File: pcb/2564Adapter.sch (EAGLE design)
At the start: 6 parts, among them IC1 TMS2564, IC2 EPROM

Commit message: !PGM/PD is a possible select pin, so add in required logic to handle correctly for all cases.
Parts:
- added IC4: 74LS00N, 74xx-us-jlb:74LS00N
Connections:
- removed net N$3: IC1A.!CS1, IC2G$1.!OE
- new net !CE: IC2G$1.!CE, IC4B.O
- new net !CS1: IC1A.!CS1, IC4A.I0, IC4A.I1
- new net !CS2: IC1A.!CS2, IC4D.I0, IC4D.I1
- new net GND: IC4C.I0, IC4C.I1
- new net N$2: IC4B.I1, IC4D.O
- new net PD: IC1A.PD/!PGM, IC2G$1.!OE
- net N$1: now also IC4A.O, IC4B.I0; no longer IC1A.!CS2, IC2G$1.!CE
- net VCC: no longer IC1A.!PGM
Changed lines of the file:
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@@
 <layer number="97" name="Info" color="7" fill="1" visible="yes" active="yes"/>
 <layer number="98" name="Guide" color="6" fill="1" visible="yes" active="yes"/>
+<layer number="99" name="SpiceOrder" color="5" fill="1" visible="yes" active="yes"/>
 <layer number="100" name="Muster" color="7" fill="1" visible="no" active="no"/>
 <layer number="101" name="Patch_Top" color="12" fill="4" visible="yes" active="yes"/>
@@
 <layer number="106" name="bPlate" color="7" fill="1" visible="yes" active="yes"/>
 <layer number="107" name="Crop" color="7" fill="1" visible="yes" active="yes"/>
+<layer number="110" name="OldCocoCase" color="7" fill="1" visible="yes" active="yes"/>
+<layer number="111" name="NewCocoCase" color="7" fill="1" visible="yes" active="yes"/>
+<layer number="112" name="C64Case" color="7" fill="1" visible="yes" active="yes"/>
 <layer number="116" name="Patch_BOT" color="9" fill="4" visible="yes" active="yes"/>
 <layer number="121" name="_tsilk" color="7" fill="1" visible="yes" active="yes"/>
@@
 <part name="IC2" library="0RB_Memory" deviceset="27512" device="'RD'" value="EPROM"/>
 <part name="IC1" library="memory-ti" deviceset="TMS2564" device="-RP" value="TMS2564"/>
-<part name="SUPPLY1" library="supply2" deviceset="VCC" device=""/>
 <part name="GOLD_ORB_SM1" library="oshw" deviceset="OSHWLOGO" device="LOGO5MM" value="Open Source Hardware"/>
+<part name="IC4" library="74xx-us-jlb" deviceset="74*00" device="N" technology="LS"/>
+<part name="SUPPLY1" library="supply2" deviceset="GND" device=""/>
 </parts>
 <sheets>
@@
 <instance part="IC2" gate="G$1" x="68.58" y="83.82"/>
 <instance part="IC1" gate="A" x="68.58" y="137.16"/>
-<instance part="SUPPLY1" gate="G$1" x="53.34" y="167.64"/>
 <instance part="GOLD_ORB_SM1" gate="G$1" x="134.62" y="15.24"/>
+<instance part="IC4" gate="A" x="134.62" y="114.3"/>
+<instance part="IC4" gate="B" x="165.1" y="104.14"/>
+<instance part="IC4" gate="C" x="134.62" y="68.58"/>
+<instance part="IC4" gate="D" x="134.62" y="93.98"/>
+<instance part="SUPPLY1" gate="GND" x="119.38" y="60.96"/>
 </instances>
 <busses>
@@
 <pinref part="SUPPLY2" gate="G$1" pin="VCC"/>
 </segment>
-<segment>
-<pinref part="SUPPLY1" gate="G$1" pin="VCC"/>
-<wire x1="53.34" y1="165.1" x2="53.34" y2="116.84" width="0.1524" layer="91"/>
-<pinref part="IC1" gate="A" pin="!PGM"/>
-<wire x1="55.88" y1="116.84" x2="53.34" y2="116.84" width="0.1524" layer="91"/>
-</segment>
 </net>
 <net name="A15" class="0">
@@
 </segment>
 </net>
-<net name="N$3" class="0">
-<segment>
-<wire x1="48.26" y1="121.92" x2="55.88" y2="121.92" width="0.1524" layer="91"/>
-<wire x1="48.26" y1="58.42" x2="55.88" y2="58.42" width="0.1524" layer="91"/>
-<wire x1="48.26" y1="121.92" x2="48.26" y2="58.42" width="0.1524" layer="91"/>
+<net name="!CS1" class="0">
+<segment>
+<pinref part="IC1" gate="A" pin="!CS1"/>
+<wire x1="55.88" y1="121.92" x2="38.1" y2="121.92" width="0.1524" layer="91"/>
+<label x="38.1" y="121.92" size="1.27" layer="95" ratio="10" rot="R180" xref="yes"/>
+</segment>
+<segment>
+<pinref part="IC4" gate="A" pin="I0"/>
+<wire x1="121.92" y1="116.84" x2="119.38" y2="116.84" width="0.1524" layer="91"/>
+<wire x1="119.38" y1="116.84" x2="119.38" y2="114.3" width="0.1524" layer="91"/>
+<pinref part="IC4" gate="A" pin="I1"/>
+<wire x1="119.38" y1="114.3" x2="119.38" y2="111.76" width="0.1524" layer="91"/>
+<wire x1="119.38" y1="111.76" x2="121.92" y2="111.76" width="0.1524" layer="91"/>
+<wire x1="119.38" y1="114.3" x2="116.84" y2="114.3" width="0.1524" layer="91"/>
+<junction x="119.38" y="114.3"/>
+<label x="116.84" y="114.3" size="1.27" layer="95" ratio="10" rot="R180" xref="yes"/>
+</segment>
+</net>
+<net name="!CS2" class="0">
+<segment>
+<pinref part="IC1" gate="A" pin="!CS2"/>
+<wire x1="55.88" y1="119.38" x2="38.1" y2="119.38" width="0.1524" layer="91"/>
+<label x="38.1" y="119.38" size="1.27" layer="95" ratio="10" rot="R180" xref="yes"/>
+</segment>
+<segment>
+<pinref part="IC4" gate="D" pin="I0"/>
+<wire x1="121.92" y1="96.52" x2="119.38" y2="96.52" width="0.1524" layer="91"/>
+<wire x1="119.38" y1="96.52" x2="119.38" y2="93.98" width="0.1524" layer="91"/>
+<pinref part="IC4" gate="D" pin="I1"/>
+<wire x1="119.38" y1="93.98" x2="119.38" y2="91.44" width="0.1524" layer="91"/>
+<wire x1="119.38" y1="91.44" x2="121.92" y2="91.44" width="0.1524" layer="91"/>
+<wire x1="119.38" y1="93.98" x2="116.84" y2="93.98" width="0.1524" layer="91"/>
+<junction x="119.38" y="93.98"/>
+<label x="116.84" y="93.98" size="1.27" layer="95" ratio="10" rot="R180" xref="yes"/>
+</segment>
+</net>
+<net name="PD" class="0">
+<segment>
+<pinref part="IC1" gate="A" pin="PD/!PGM"/>
+<wire x1="55.88" y1="116.84" x2="38.1" y2="116.84" width="0.1524" layer="91"/>
+<label x="38.1" y="116.84" size="1.27" layer="95" ratio="10" rot="R180" xref="yes"/>
+</segment>
+<segment>
 <pinref part="IC2" gate="G$1" pin="!OE"/>
-<pinref part="IC1" gate="A" pin="!CS1"/>
+<wire x1="38.1" y1="58.42" x2="55.88" y2="58.42" width="0.1524" layer="91"/>
+<label x="38.1" y="58.42" size="1.27" layer="95" ratio="10" rot="R180" xref="yes"/>
+</segment>
+</net>
+<net name="!CE" class="0">
+<segment>
+<pinref part="IC2" gate="G$1" pin="!CE"/>
+<wire x1="55.88" y1="60.96" x2="38.1" y2="60.96" width="0.1524" layer="91"/>
+<label x="38.1" y="60.96" size="1.27" layer="95" ratio="10" rot="R180" xref="yes"/>
+</segment>
+<segment>
+<pinref part="IC4" gate="B" pin="O"/>
+<wire x1="177.8" y1="104.14" x2="180.34" y2="104.14" width="0.1524" layer="91"/>
+<label x="180.34" y="104.14" size="1.27" layer="95" ratio="10" xref="yes"/>
 </segment>
 </net>
 <net name="N$1" class="0">
 <segment>
-<pinref part="IC2" gate="G$1" pin="!CE"/>
-<pinref part="IC1" gate="A" pin="!CS2"/>
-<wire x1="55.88" y1="119.38" x2="50.8" y2="119.38" width="0.1524" layer="91"/>
-<wire x1="50.8" y1="119.38" x2="50.8" y2="60.96" width="0.1524" layer="91"/>
-<wire x1="50.8" y1="60.96" x2="55.88" y2="60.96" width="0.1524" layer="91"/>
-</segment>
-</net>
+<pinref part="IC4" gate="A" pin="O"/>
+<wire x1="147.32" y1="114.3" x2="149.86" y2="114.3" width="0.1524" layer="91"/>
+<wire x1="149.86" y1="114.3" x2="149.86" y2="106.68" width="0.1524" layer="91"/>
+<pinref part="IC4" gate="B" pin="I0"/>
+<wire x1="149.86" y1="106.68" x2="152.4" y2="106.68" width="0.1524" layer="91"/>
+</segment>
+</net>
+<net name="N$2" class="0">
+<segment>
+<pinref part="IC4" gate="B" pin="I1"/>
+<wire x1="152.4" y1="101.6" x2="149.86" y2="101.6" width="0.1524" layer="91"/>
+<wire x1="149.86" y1="101.6" x2="149.86" y2="93.98" width="0.1524" layer="91"/>
+<pinref part="IC4" gate="D" pin="O"/>
+<wire x1="149.86" y1="93.98" x2="147.32" y2="93.98" width="0.1524" layer="91"/>
+</segment>
+</net>
+<net name="GND" class="0">
+<segment>
+<pinref part="IC4" gate="C" pin="I0"/>
+<wire x1="121.92" y1="71.12" x2="119.38" y2="71.12" width="0.1524" layer="91"/>
+<wire x1="119.38" y1="71.12" x2="119.38" y2="66.04" width="0.1524" layer="91"/>
+<pinref part="SUPPLY1" gate="GND" pin="GND"/>
+<pinref part="IC4" gate="C" pin="I1"/>
+<wire x1="119.38" y1="66.04" x2="119.38" y2="63.5" width="0.1524" layer="91"/>
+<wire x1="121.92" y1="66.04" x2="119.38" y2="66.04" width="0.1524" layer="91"/>
+<junction x="119.38" y="66.04"/>
+</segment>
+</net>

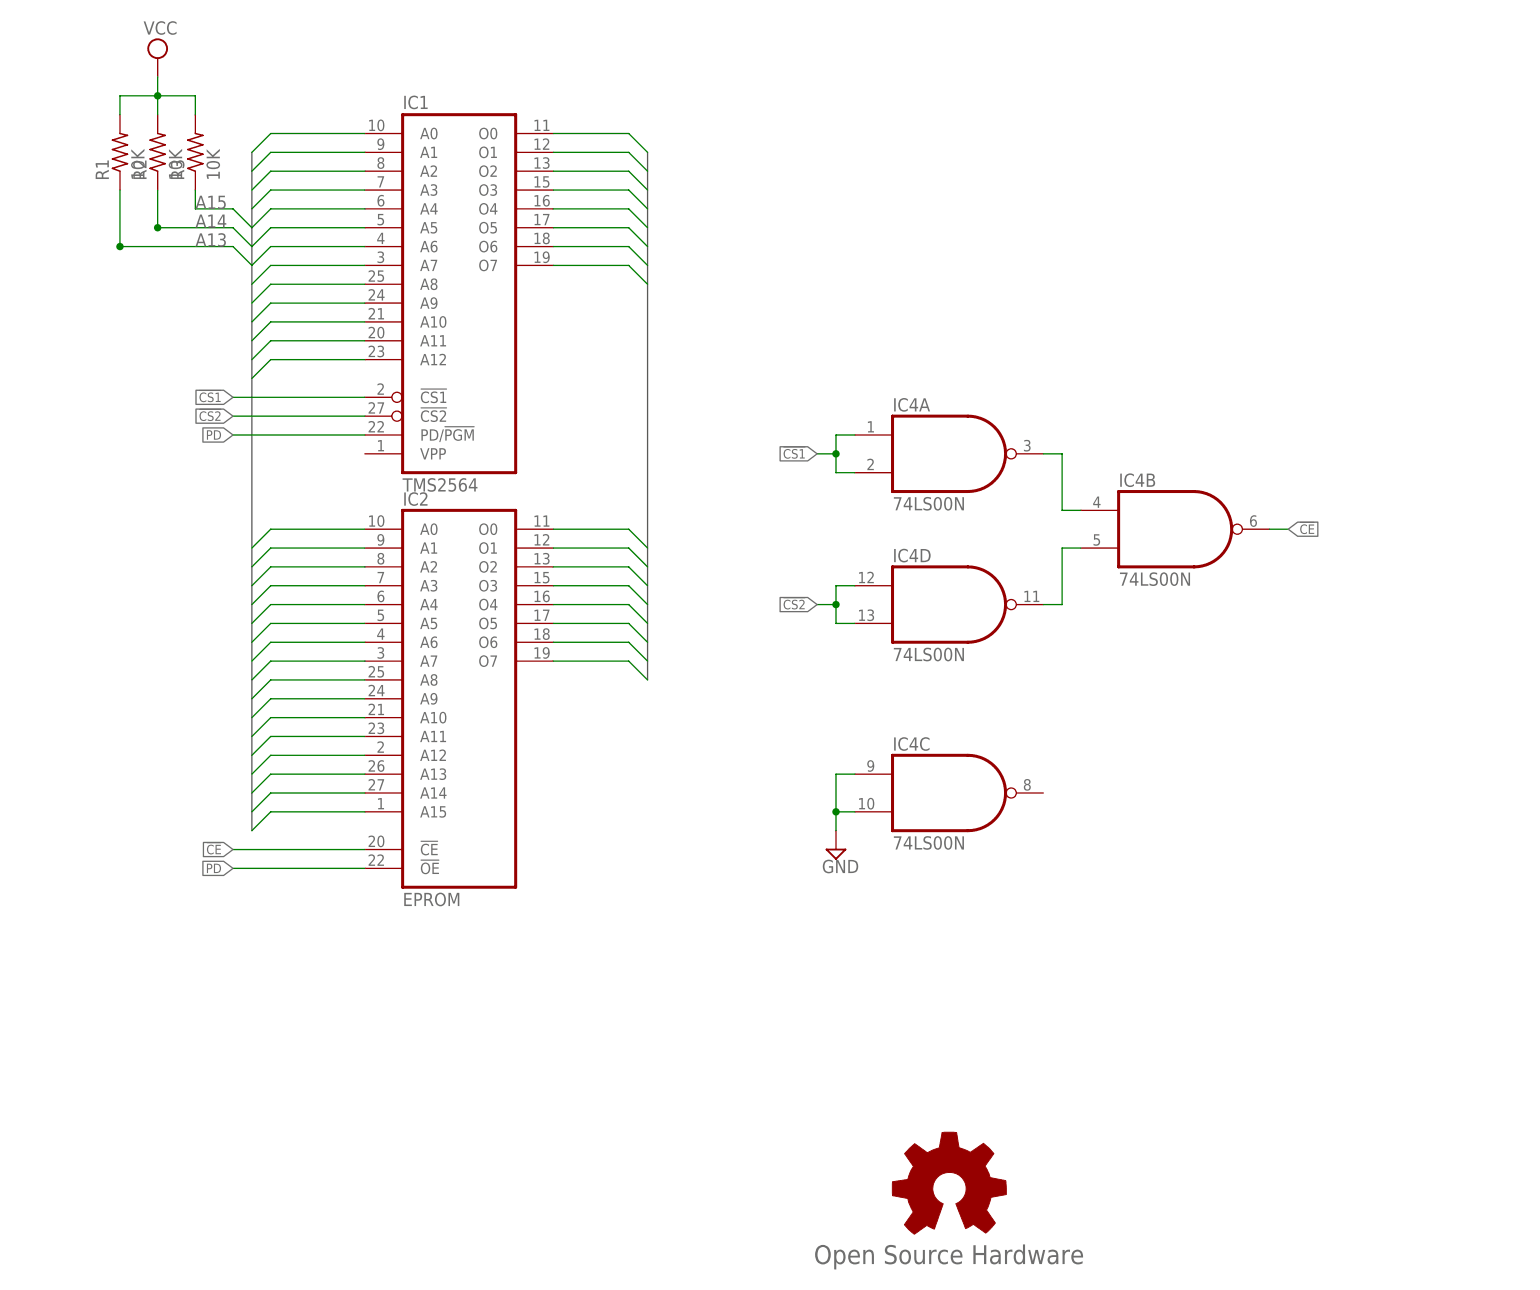
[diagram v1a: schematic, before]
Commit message: PCB Updates and BOM cleanup
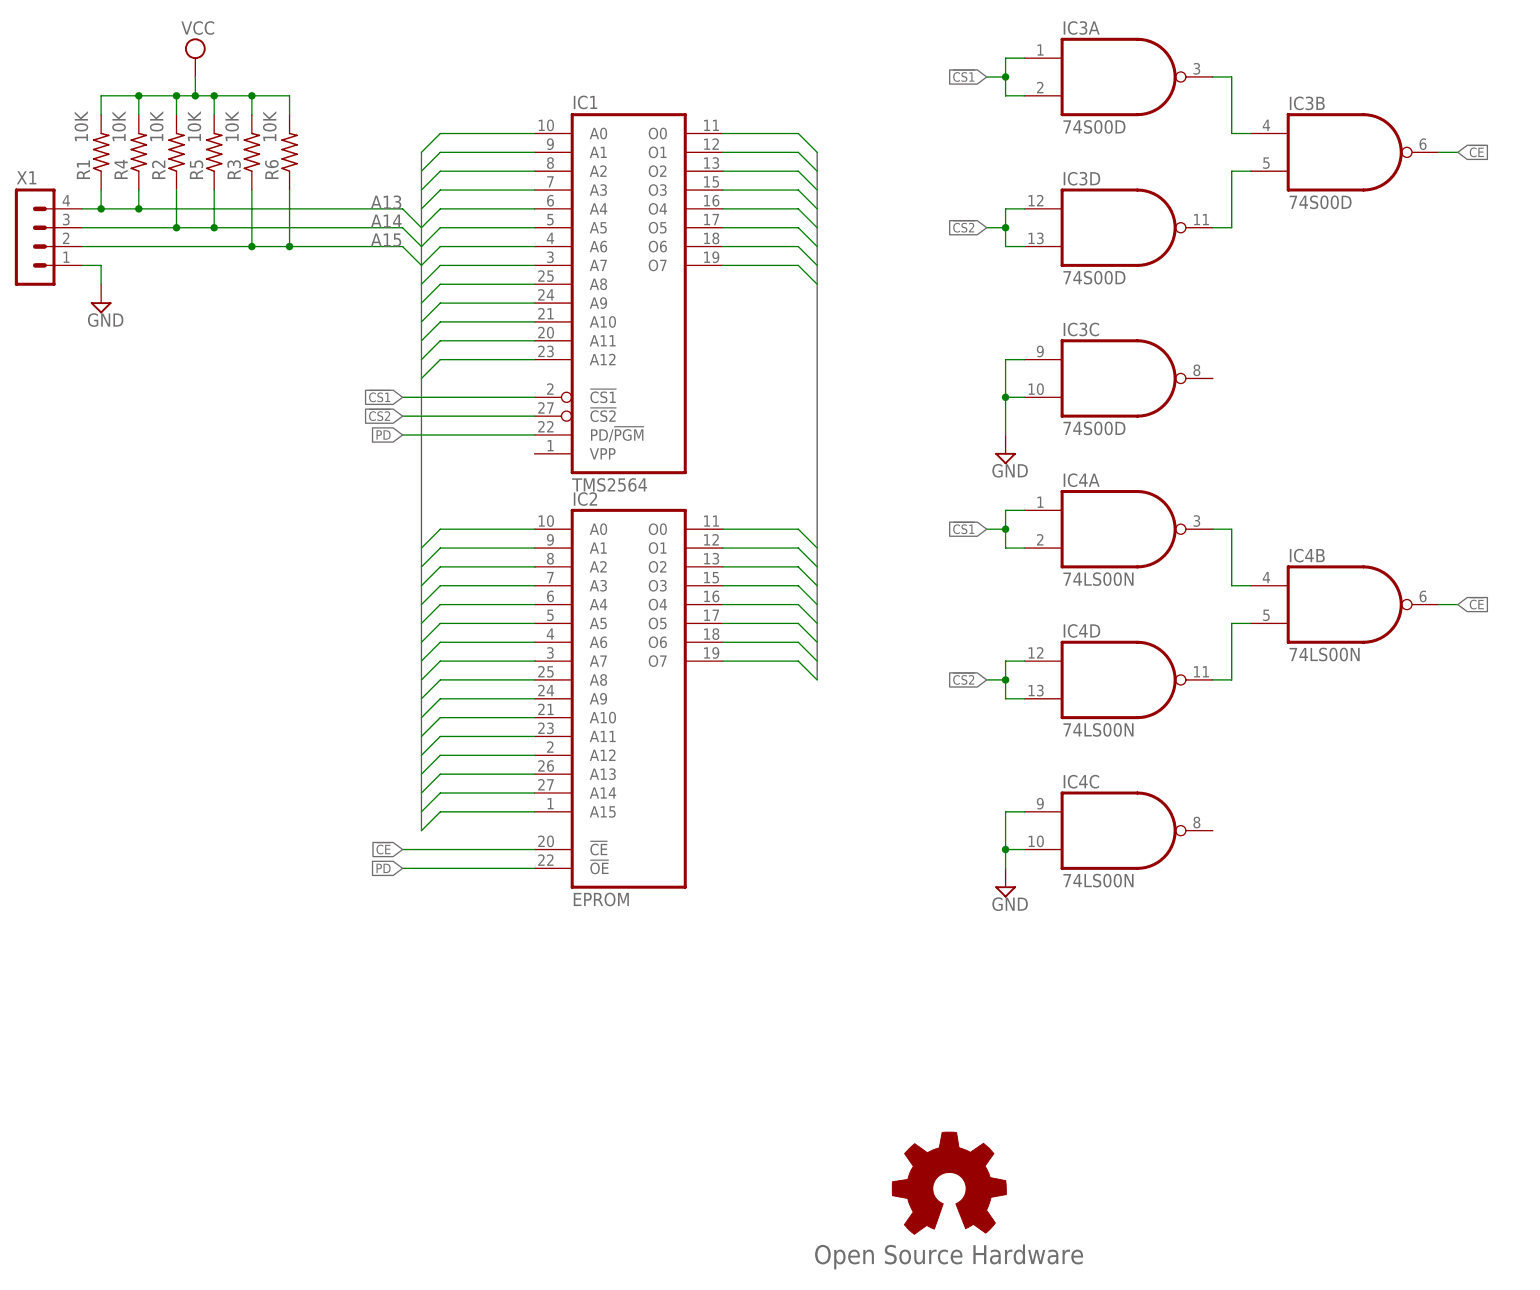
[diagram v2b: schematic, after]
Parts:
- added IC3: 74S00D, 74xx-us:74S00D
- added R4, R5, R6: 10K, resistor:R-US_R0805
- added X1: (no value), con-lstb-rp:MA04-1
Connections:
- new net N$3: IC3A.O, IC3B.I0
- new net N$4: IC3B.I1, IC3D.O
- net !CE: now also IC3B.O
- net !CS1: now also IC3A.I0, IC3A.I1
- net !CS2: now also IC3D.I0, IC3D.I1
- net A13: now also R4.1, X1.4
- net A14: now also R5.1, X1.3
- net A15: now also R6.1, X1.2
- net GND: now also IC3C.I0, IC3C.I1, X1.1
- net VCC: now also R4.2, R5.2, R6.2
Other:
- moved on the sheet: IC1, IC2, IC4A, IC4B, IC4C, IC4D, R1, R2, R3
